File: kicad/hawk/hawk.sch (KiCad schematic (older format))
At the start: 10 parts, among them J1 GPIO_AA, J2 GPIO_BB, J3 SWD_PGM, SW1 SW_Push, U1 ATSAMD10C14A-SS

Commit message: [KICAD] Hawk tutorial pt. 2
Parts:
- added C2, C3: 1uF, symbol Device:C_Small
- added J4: Battery, Connector_JST:JST_PH_B2B-PH-K_1x02_P2.00mm_Vertical, symbol Connector_Generic:Conn_01x02
- added U2: AP7333-33SRG-7, Package_TO_SOT_SMD:SOT-23, symbol Regulator_Linear:APE8865N-12-HF-3
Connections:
- net +3V3: now also C3.1, U2.2 (VO)
- net GND: now also C2.2, C3.2, J4.2 (Pin_2)
- new net +BATT: C2.1, J4.1 (Pin_1), U2.3 (VI)
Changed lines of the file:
@@
 	7700 5550 7700 5700
 $Comp
-L power:+3V3 #PWR?
+L power:+3V3 #PWR015
 U 1 1 605063F1
 P 6450 4950
-F 0 "#PWR?" H 6450 4800 50  0001 C CNN
+F 0 "#PWR015" H 6450 4800 50  0001 C CNN
 F 1 "+3V3" H 6465 5123 50  0000 C CNN
 F 2 "" H 6450 4950 50  0001 C CNN
@@
 Wire Wire Line
 	6450 5150 6650 5150
+$Comp
+L Connector_Generic:Conn_01x02 J4
+U 1 1 60507C0C
+P 2700 5250
+F 0 "J4" H 2780 5242 50  0000 L CNN
+F 1 "Battery" H 2780 5151 50  0000 L CNN
+F 2 "Connector_JST:JST_PH_B2B-PH-K_1x02_P2.00mm_Vertical" H 2700 5250 50  0001 C CNN
+F 3 "~" H 2700 5250 50  0001 C CNN
+	1    2700 5250
+	1    0    0    -1
+$EndComp
+$Comp
+L Regulator_Linear:APE8865N-12-HF-3 U2
+U 1 1 60511020
+P 1450 5350
+F 0 "U2" H 1450 5592 50  0000 C CNN
+F 1 "AP7333-33SRG-7" H 1450 5501 50  0000 C CNN
+F 2 "Package_TO_SOT_SMD:SOT-23" H 1450 5575 50  0001 C CIN
+F 3 "http://www.tme.eu/fr/Document/ced3461ed31ea70a3c416fb648e0cde7/APE8865-3.pdf" H 1450 5350 50  0001 C CNN
+	1    1450 5350
+	1    0    0    -1
+$EndComp
+$Comp
+L Device:C_Small C3
+U 1 1 60512C46
+P 1950 5500
+F 0 "C3" H 2042 5546 50  0000 L CNN
+F 1 "1uF" H 2042 5455 50  0000 L CNN
+F 2 "" H 1950 5500 50  0001 C CNN
+F 3 "~" H 1950 5500 50  0001 C CNN
+	1    1950 5500
+	1    0    0    -1
+$EndComp
+$Comp
+L Device:C_Small C2
+U 1 1 60514DD0
+P 800 5550
+F 0 "C2" H 892 5596 50  0000 L CNN
+F 1 "1uF" H 892 5505 50  0000 L CNN
+F 2 "" H 800 5550 50  0001 C CNN
+F 3 "~" H 800 5550 50  0001 C CNN
+	1    800  5550
+	1    0    0    -1
+$EndComp
+$Comp
+L power:GND #PWR012
+U 1 1 6051789F
+P 800 5900
+F 0 "#PWR012" H 800 5650 50  0001 C CNN
+F 1 "GND" H 805 5727 50  0000 C CNN
+F 2 "" H 800 5900 50  0001 C CNN
+F 3 "" H 800 5900 50  0001 C CNN
+	1    800  5900
+	1    0    0    -1
+$EndComp
+$Comp
+L power:GND #PWR014
+U 1 1 60519549
+P 1950 5900
+F 0 "#PWR014" H 1950 5650 50  0001 C CNN
+F 1 "GND" H 1955 5727 50  0000 C CNN
+F 2 "" H 1950 5900 50  0001 C CNN
+F 3 "" H 1950 5900 50  0001 C CNN
+	1    1950 5900
+	1    0    0    -1
+$EndComp
+Wire Wire Line
+	1150 5350 800  5350
+Wire Wire Line
+	800  5350 800  5450
+Wire Wire Line
+	1750 5350 1950 5350
+Wire Wire Line
+	1950 5350 1950 5400
+Wire Wire Line
+	1950 5600 1950 5900
+Wire Wire Line
+	800  5650 800  5900
+$Comp
+L power:+3V3 #PWR013
+U 1 1 6051A8E4
+P 1950 5350
+F 0 "#PWR013" H 1950 5200 50  0001 C CNN
+F 1 "+3V3" H 1965 5523 50  0000 C CNN
+F 2 "" H 1950 5350 50  0001 C CNN
+F 3 "" H 1950 5350 50  0001 C CNN
+	1    1950 5350
+	1    0    0    -1
+$EndComp
+Connection ~ 1950 5350
+$Comp
+L power:+BATT #PWR?
+U 1 1 6051B4BB
+P 2500 5250
+F 0 "#PWR?" H 2500 5100 50  0001 C CNN
+F 1 "+BATT" H 2515 5423 50  0000 C CNN
+F 2 "" H 2500 5250 50  0001 C CNN
+F 3 "" H 2500 5250 50  0001 C CNN
+	1    2500 5250
+	1    0    0    -1
+$EndComp
+$Comp
+L power:+BATT #PWR?
+U 1 1 6051BB44
+P 800 5350
+F 0 "#PWR?" H 800 5200 50  0001 C CNN
+F 1 "+BATT" H 815 5523 50  0000 C CNN
+F 2 "" H 800 5350 50  0001 C CNN
+F 3 "" H 800 5350 50  0001 C CNN
+	1    800  5350
+	1    0    0    -1
+$EndComp
+Connection ~ 800  5350
+$Comp
+L power:GND #PWR?
+U 1 1 6051C01F
+P 2500 5350
+F 0 "#PWR?" H 2500 5100 50  0001 C CNN
+F 1 "GND" H 2505 5177 50  0000 C CNN
+F 2 "" H 2500 5350 50  0001 C CNN
+F 3 "" H 2500 5350 50  0001 C CNN
+	1    2500 5350
+	1    0    0    -1
+$EndComp
 $EndSCHEMATC

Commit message: [KICAD] Hawk tutorial pt. 3
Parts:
- C1, C2, C3: footprint (none) -> Capacitor_SMD:C_0805_2012Metric_Pad1.15x1.40mm_HandSolder
- D1: footprint (none) -> LED_SMD:LED_0805_2012Metric_Pad1.15x1.40mm_HandSolder
- J1, J2: footprint (none) -> Connector_PinHeader_2.54mm:PinHeader_1x05_P2.54mm_Vertical
- J3: footprint (none) -> Connector_PinHeader_2.54mm:PinHeader_2x03_P2.54mm_Vertical
- R1, R2, R3: footprint (none) -> Resistor_SMD:R_0805_2012Metric_Pad1.15x1.40mm_HandSolder
- SW1: footprint (none) -> Button_Switch_THT:SW_PUSH_6mm
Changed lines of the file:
@@
 F 0 "C1" H 6092 2696 50  0000 L CNN
 F 1 "0.1uf" H 6092 2605 50  0000 L CNN
-F 2 "" H 6000 2650 50  0001 C CNN
+F 2 "Capacitor_SMD:C_0805_2012Metric_Pad1.15x1.40mm_HandSolder" H 6000 2650 50  0001 C CNN
 F 3 "~" H 6000 2650 50  0001 C CNN
 	1    6000 2650
@@
 F 0 "R1" H 6720 2696 50  0000 L CNN
 F 1 "10k" H 6720 2605 50  0000 L CNN
-F 2 "" V 6580 2650 50  0001 C CNN
+F 2 "Resistor_SMD:R_0805_2012Metric_Pad1.15x1.40mm_HandSolder" V 6580 2650 50  0001 C CNN
 F 3 "~" H 6650 2650 50  0001 C CNN
 	1    6650 2650
@@
 F 0 "SW1" H 3850 2735 50  0000 C CNN
 F 1 "SW_Push" H 3850 2644 50  0000 C CNN
-F 2 "" H 3850 2650 50  0001 C CNN
+F 2 "Button_Switch_THT:SW_PUSH_6mm" H 3850 2650 50  0001 C CNN
 F 3 "~" H 3850 2650 50  0001 C CNN
 	1    3850 2450
@@
 F 0 "D1" H 6893 3545 50  0000 C CNN
 F 1 "LED_ALT" H 6893 3636 50  0000 C CNN
-F 2 "" H 6900 3800 50  0001 C CNN
+F 2 "LED_SMD:LED_0805_2012Metric_Pad1.15x1.40mm_HandSolder" H 6900 3800 50  0001 C CNN
 F 3 "~" H 6900 3800 50  0001 C CNN
 	1    6900 3800
@@
 F 0 "R2" V 7193 3800 50  0000 C CNN
 F 1 "1k" V 7284 3800 50  0000 C CNN
-F 2 "" V 7330 3800 50  0001 C CNN
+F 2 "Resistor_SMD:R_0805_2012Metric_Pad1.15x1.40mm_HandSolder" V 7330 3800 50  0001 C CNN
 F 3 "~" H 7400 3800 50  0001 C CNN
 	1    7400 3800
@@
 F 0 "J3" H 8000 3417 50  0000 C CNN
 F 1 "SWD_PGM" H 8000 3326 50  0000 C CNN
-F 2 "" H 7950 3100 50  0001 C CNN
+F 2 "Connector_PinHeader_2.54mm:PinHeader_2x03_P2.54mm_Vertical" H 7950 3100 50  0001 C CNN
 F 3 "~" H 7950 3100 50  0001 C CNN
 	1    7950 3100
@@
 F 0 "R3" H 3920 3596 50  0000 L CNN
 F 1 "1k" H 3920 3505 50  0000 L CNN
-F 2 "" V 3780 3550 50  0001 C CNN
+F 2 "Resistor_SMD:R_0805_2012Metric_Pad1.15x1.40mm_HandSolder" V 3780 3550 50  0001 C CNN
 F 3 "~" H 3850 3550 50  0001 C CNN
 	1    3850 3550
@@
 F 0 "J1" H 6930 5392 50  0000 L CNN
 F 1 "GPIO_AA" H 6930 5301 50  0000 L CNN
-F 2 "" H 6850 5350 50  0001 C CNN
+F 2 "Connector_PinHeader_2.54mm:PinHeader_1x05_P2.54mm_Vertical" H 6850 5350 50  0001 C CNN
 F 3 "~" H 6850 5350 50  0001 C CNN
 	1    6850 5350
@@
 F 0 "J2" H 7268 4925 50  0000 C CNN
 F 1 "GPIO_BB" H 7268 5016 50  0000 C CNN
-F 2 "" H 7350 5350 50  0001 C CNN
+F 2 "Connector_PinHeader_2.54mm:PinHeader_1x05_P2.54mm_Vertical" H 7350 5350 50  0001 C CNN
 F 3 "~" H 7350 5350 50  0001 C CNN
 	1    7350 5350
@@
 F 0 "C3" H 2042 5546 50  0000 L CNN
 F 1 "1uF" H 2042 5455 50  0000 L CNN
-F 2 "" H 1950 5500 50  0001 C CNN
+F 2 "Capacitor_SMD:C_0805_2012Metric_Pad1.15x1.40mm_HandSolder" H 1950 5500 50  0001 C CNN
 F 3 "~" H 1950 5500 50  0001 C CNN
 	1    1950 5500
@@
 F 0 "C2" H 892 5596 50  0000 L CNN
 F 1 "1uF" H 892 5505 50  0000 L CNN
-F 2 "" H 800 5550 50  0001 C CNN
+F 2 "Capacitor_SMD:C_0805_2012Metric_Pad1.15x1.40mm_HandSolder" H 800 5550 50  0001 C CNN
 F 3 "~" H 800 5550 50  0001 C CNN
 	1    800  5550

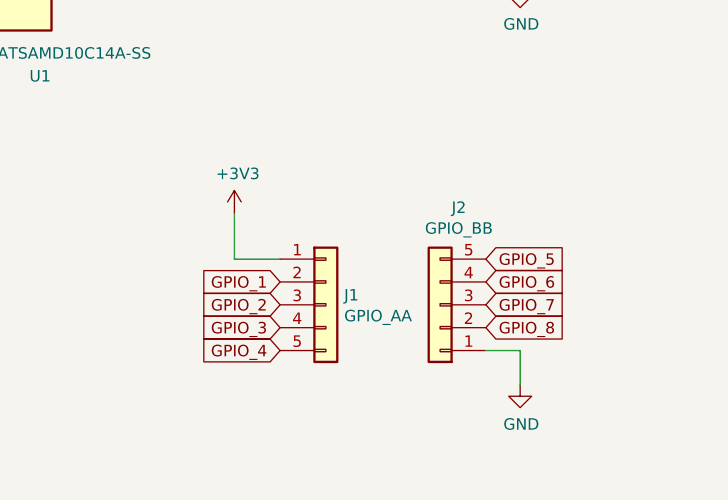
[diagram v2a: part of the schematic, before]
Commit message: [KICAD] Hawk tutorial pt. 5-8
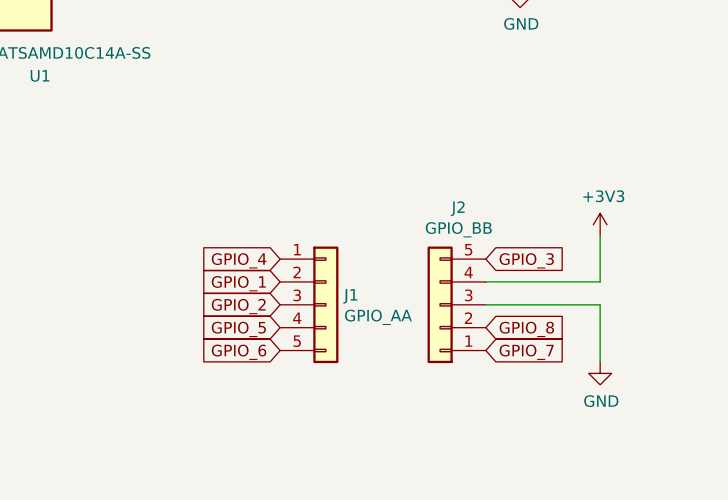
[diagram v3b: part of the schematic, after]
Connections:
- net +3V3: now also J2.4 (Pin_4); no longer J1.1 (Pin_1)
- net GND: now also J2.3 (Pin_3); no longer J2.1 (Pin_1)
- net GPIO_3: now also J2.5 (Pin_5); no longer J1.4 (Pin_4)
- net GPIO_4: now also J1.1 (Pin_1); no longer J1.5 (Pin_5)
- net GPIO_5: now also J1.4 (Pin_4); no longer J2.5 (Pin_5)
- net GPIO_6: now also J1.5 (Pin_5); no longer J2.4 (Pin_4)
- net GPIO_7: now also J2.1 (Pin_1); no longer J2.3 (Pin_3)
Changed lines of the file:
@@
 Text GLabel 6650 5350 0    50   Input ~ 0
 GPIO_2
-Text GLabel 6650 5450 0    50   Input ~ 0
-GPIO_3
 Text GLabel 6650 5550 0    50   Input ~ 0
-GPIO_4
-Text GLabel 7550 5150 2    50   Input ~ 0
-GPIO_5
-Text GLabel 7550 5250 2    50   Input ~ 0
 GPIO_6
-Text GLabel 7550 5350 2    50   Input ~ 0
+Text GLabel 7550 5550 2    50   Input ~ 0
 GPIO_7
 Text GLabel 7550 5450 2    50   Input ~ 0
@@
 L power:GND #PWR011
 U 1 1 60502D29
-P 7700 5700
-F 0 "#PWR011" H 7700 5450 50  0001 C CNN
-F 1 "GND" H 7705 5527 50  0000 C CNN
-F 2 "" H 7700 5700 50  0001 C CNN
-F 3 "" H 7700 5700 50  0001 C CNN
-	1    7700 5700
+P 8050 5600
+F 0 "#PWR011" H 8050 5350 50  0001 C CNN
+F 1 "GND" H 8055 5427 50  0000 C CNN
+F 2 "" H 8050 5600 50  0001 C CNN
+F 3 "" H 8050 5600 50  0001 C CNN
+	1    8050 5600
 	1    0    0    -1
 $EndComp
-Wire Wire Line
-	7550 5550 7700 5550
-Wire Wire Line
-	7700 5550 7700 5700
 $Comp
 L power:+3V3 #PWR015
 U 1 1 605063F1
-P 6450 4950
-F 0 "#PWR015" H 6450 4800 50  0001 C CNN
-F 1 "+3V3" H 6465 5123 50  0000 C CNN
-F 2 "" H 6450 4950 50  0001 C CNN
-F 3 "" H 6450 4950 50  0001 C CNN
-	1    6450 4950
+P 8050 5050
+F 0 "#PWR015" H 8050 4900 50  0001 C CNN
+F 1 "+3V3" H 8065 5223 50  0000 C CNN
+F 2 "" H 8050 5050 50  0001 C CNN
+F 3 "" H 8050 5050 50  0001 C CNN
+	1    8050 5050
 	1    0    0    -1
 $EndComp
-Wire Wire Line
-	6450 4950 6450 5150
-Wire Wire Line
-	6450 5150 6650 5150
 $Comp
 L Connector_Generic:Conn_01x02 J4
@@
 Connection ~ 1950 5350
 $Comp
-L power:+BATT #PWR?
+L power:+BATT #PWR0101
 U 1 1 6051B4BB
 P 2500 5250
-F 0 "#PWR?" H 2500 5100 50  0001 C CNN
+F 0 "#PWR0101" H 2500 5100 50  0001 C CNN
 F 1 "+BATT" H 2515 5423 50  0000 C CNN
 F 2 "" H 2500 5250 50  0001 C CNN
@@
 $EndComp
 $Comp
-L power:+BATT #PWR?
+L power:+BATT #PWR0102
 U 1 1 6051BB44
 P 800 5350
-F 0 "#PWR?" H 800 5200 50  0001 C CNN
+F 0 "#PWR0102" H 800 5200 50  0001 C CNN
 F 1 "+BATT" H 815 5523 50  0000 C CNN
 F 2 "" H 800 5350 50  0001 C CNN
@@
 Connection ~ 800  5350
 $Comp
-L power:GND #PWR?
+L power:GND #PWR0103
 U 1 1 6051C01F
 P 2500 5350
-F 0 "#PWR?" H 2500 5100 50  0001 C CNN
+F 0 "#PWR0103" H 2500 5100 50  0001 C CNN
 F 1 "GND" H 2505 5177 50  0000 C CNN
 F 2 "" H 2500 5350 50  0001 C CNN
@@
 	1    0    0    -1
 $EndComp
+Text GLabel 6650 5450 0    50   Input ~ 0
+GPIO_5
+Text GLabel 7550 5150 2    50   Input ~ 0
+GPIO_3
+Text GLabel 6650 5150 0    50   Input ~ 0
+GPIO_4
+Wire Wire Line
+	8050 5050 8050 5250
+Wire Wire Line
+	8050 5250 7550 5250
+Wire Wire Line
+	8050 5600 8050 5350
+Wire Wire Line
+	8050 5350 7550 5350
 $EndSCHEMATC
